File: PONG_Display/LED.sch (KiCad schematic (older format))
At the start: 4 parts, among them J1 LED_Display_Conn, U1 PC817

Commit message: 5v
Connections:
- net labels added: +5V
- net labels removed: +12V
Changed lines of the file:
@@
 EESchema Schematic File Version 4
-LIBS:PONG_Display-cache
 EELAYER 30 0
 EELAYER END
@@
 Schemat wyświetlacza LED
 $Comp
-L power:+12V #PWR0101
-U 1 1 5E85B748
-P 8500 2550
-F 0 "#PWR0101" H 8500 2400 50  0001 C CNN
-F 1 "+12V" H 8515 2723 50  0000 C CNN
-F 2 "" H 8500 2550 50  0001 C CNN
-F 3 "" H 8500 2550 50  0001 C CNN
-	1    8500 2550
-	1    0    0    -1
-$EndComp
-$Comp
-L power:GND #PWR0102
+L power:GND #PWR05
 U 1 1 5E85BD1D
 P 8500 3050
-F 0 "#PWR0102" H 8500 2800 50  0001 C CNN
+F 0 "#PWR05" H 8500 2800 50  0001 C CNN
 F 1 "GND" H 8505 2877 50  0000 C CNN
 F 2 "" H 8500 3050 50  0001 C CNN
@@
 $EndComp
 $Comp
-L power:GND #PWR0103
+L power:GND #PWR01
 U 1 1 5E9048A0
 P 2450 3200
-F 0 "#PWR0103" H 2450 2950 50  0001 C CNN
+F 0 "#PWR01" H 2450 2950 50  0001 C CNN
 F 1 "GND" H 2455 3027 50  0000 C CNN
 F 2 "" H 2450 3200 50  0001 C CNN
@@
 $EndComp
 $Comp
-L power:GND #PWR0105
+L power:GND #PWR02
 U 1 1 5E906F7A
 P 3400 3200
-F 0 "#PWR0105" H 3400 2950 50  0001 C CNN
+F 0 "#PWR02" H 3400 2950 50  0001 C CNN
 F 1 "GND" H 3405 3027 50  0000 C CNN
 F 2 "" H 3400 3200 50  0001 C CNN
@@
 	1900 2550 2050 2550
 $Comp
-L power:+12V #PWR0104
-U 1 1 5E9C9DE1
+L power:+5V #PWR?
+U 1 1 5EA0B092
+P 8500 2550
+AR Path="/5E80B14C/5EA0B092" Ref="#PWR?"  Part="1"
+AR Path="/5E80C133/5EA0B092" Ref="#PWR04"  Part="1"
+F 0 "#PWR04" H 8500 2400 50  0001 C CNN
+F 1 "+5V" H 8515 2723 50  0000 C CNN
+F 2 "" H 8500 2550 50  0001 C CNN
+F 3 "" H 8500 2550 50  0001 C CNN
+	1    8500 2550
+	1    0    0    -1
+$EndComp
+$Comp
+L power:+5V #PWR?
+U 1 1 5EA0B611
 P 3500 2300
-F 0 "#PWR0104" H 3500 2150 50  0001 C CNN
-F 1 "+12V" H 3515 2473 50  0000 C CNN
+AR Path="/5E80B14C/5EA0B611" Ref="#PWR?"  Part="1"
+AR Path="/5E80C133/5EA0B611" Ref="#PWR03"  Part="1"
+F 0 "#PWR03" H 3500 2150 50  0001 C CNN
+F 1 "+5V" H 3515 2473 50  0000 C CNN
 F 2 "" H 3500 2300 50  0001 C CNN
 F 3 "" H 3500 2300 50  0001 C CNN

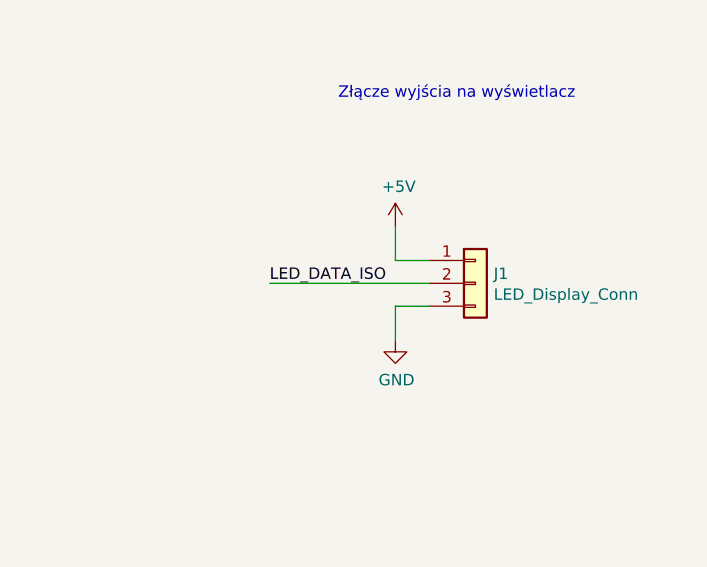
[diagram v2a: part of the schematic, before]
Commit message: dodalem rezystory i wywalilem ze zlacza zasilanie tasmy
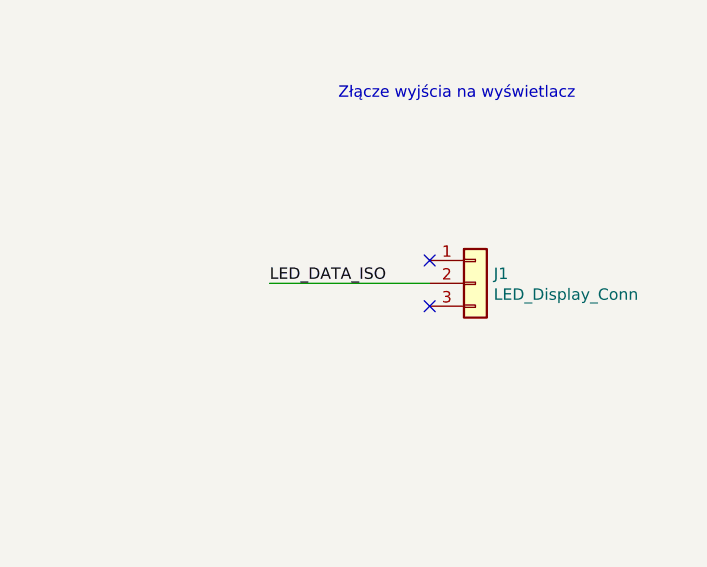
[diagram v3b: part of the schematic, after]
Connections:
- net +5V: no longer J1.1 (Pin_1)
- net GND: no longer J1.3 (Pin_3)
- no-connect marks 0 -> 2
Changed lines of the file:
@@
 Text Notes 7750 7500 0    50   ~ 0
 Schemat wyświetlacza LED
-$Comp
-L power:GND #PWR05
-U 1 1 5E85BD1D
-P 8500 3050
-F 0 "#PWR05" H 8500 2800 50  0001 C CNN
-F 1 "GND" H 8505 2877 50  0000 C CNN
-F 2 "" H 8500 3050 50  0001 C CNN
-F 3 "" H 8500 3050 50  0001 C CNN
-	1    8500 3050
-	1    0    0    -1
-$EndComp
-Wire Wire Line
-	8500 2550 8500 2700
-Wire Wire Line
-	8500 2700 8650 2700
-Wire Wire Line
-	8500 2900 8500 3050
-Wire Wire Line
-	8500 2900 8650 2900
 Text Notes 8250 2000 0    50   ~ 0
 Złącze wyjścia na wyświetlacz
@@
 $Comp
 L power:+5V #PWR?
-U 1 1 5EA0B092
-P 8500 2550
-AR Path="/5E80B14C/5EA0B092" Ref="#PWR?"  Part="1"
-AR Path="/5E80C133/5EA0B092" Ref="#PWR04"  Part="1"
-F 0 "#PWR04" H 8500 2400 50  0001 C CNN
-F 1 "+5V" H 8515 2723 50  0000 C CNN
-F 2 "" H 8500 2550 50  0001 C CNN
-F 3 "" H 8500 2550 50  0001 C CNN
-	1    8500 2550
-	1    0    0    -1
-$EndComp
-$Comp
-L power:+5V #PWR?
 U 1 1 5EA0B611
 P 3500 2300
@@
 	1    0    0    -1
 $EndComp
+NoConn ~ 8650 2700
+NoConn ~ 8650 2900
 $EndSCHEMATC

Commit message: layout v1
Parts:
- C1: footprint Capacitor_SMD:C_1206_3216Metric_Pad1.42x1.75mm_HandSolder -> Capacitor_SMD:C_0603_1608Metric_Pad1.05x0.95mm_HandSolder
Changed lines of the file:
@@
 EESchema Schematic File Version 4
-LIBS:PONG_Display-cache
 EELAYER 30 0
 EELAYER END
@@
 F 0 "C1" H 3515 2996 50  0000 L CNN
 F 1 "100n" H 3515 2905 50  0000 L CNN
-F 2 "Capacitor_SMD:C_1206_3216Metric_Pad1.42x1.75mm_HandSolder" H 3438 2800 50  0001 C CNN
+F 2 "Capacitor_SMD:C_0603_1608Metric_Pad1.05x0.95mm_HandSolder" H 3438 2800 50  0001 C CNN
 F 3 "~" H 3400 2950 50  0001 C CNN
 	1    3400 2950

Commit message: l
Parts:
- R1: footprint Resistor_SMD:R_1206_3216Metric_Pad1.42x1.75mm_HandSolder -> Resistor_SMD:R_0603_1608Metric_Pad1.05x0.95mm_HandSolder
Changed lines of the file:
@@
 F 0 "R1" V 1993 2550 50  0000 C CNN
 F 1 "180R" V 2084 2550 50  0000 C CNN
-F 2 "Resistor_SMD:R_1206_3216Metric_Pad1.42x1.75mm_HandSolder" V 2130 2550 50  0001 C CNN
+F 2 "Resistor_SMD:R_0603_1608Metric_Pad1.05x0.95mm_HandSolder" V 2130 2550 50  0001 C CNN
 F 3 "~" H 2200 2550 50  0001 C CNN
 	1    2200 2550

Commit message: layout4
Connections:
- net GND: now also J1.1 (Pin_1)
- net +5VA: now reaches J1.3 (Pin_3)
- no-connect marks 2 -> 0
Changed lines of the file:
@@
 F 3 "~" H 8850 2800 50  0001 C CNN
 	1    8850 2800
-	1    0    0    -1
+	1    0    0    1
 $EndComp
 Text Notes 7750 7500 0    50   ~ 0
@@
 	1    0    0    -1
 $EndComp
-NoConn ~ 8650 2700
-NoConn ~ 8650 2900
+$Comp
+L power:GND #PWR0109
+U 1 1 5EB33F3E
+P 8600 3100
+F 0 "#PWR0109" H 8600 2850 50  0001 C CNN
+F 1 "GND" H 8605 2927 50  0000 C CNN
+F 2 "" H 8600 3100 50  0001 C CNN
+F 3 "" H 8600 3100 50  0001 C CNN
+	1    8600 3100
+	1    0    0    -1
+$EndComp
+Wire Wire Line
+	8600 2500 8600 2700
+Wire Wire Line
+	8600 2700 8650 2700
+Wire Wire Line
+	8600 3100 8600 2900
+Wire Wire Line
+	8600 2900 8650 2900
+$Comp
+L power:+5VA #PWR0110
+U 1 1 5EA4877F
+P 8600 2500
+F 0 "#PWR0110" H 8600 2350 50  0001 C CNN
+F 1 "+5VA" H 8615 2673 50  0000 C CNN
+F 2 "" H 8600 2500 50  0001 C CNN
+F 3 "" H 8600 2500 50  0001 C CNN
+	1    8600 2500
+	1    0    0    -1
+$EndComp
 $EndSCHEMATC

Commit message: laayout6
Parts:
- J1: footprint TerminalBlock:TerminalBlock_bornier-3_P5.08mm -> TerminalBlock_RND:TerminalBlock_RND_205-00002_1x03_P5.00mm_Horizontal
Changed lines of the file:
@@
 F 0 "J1" H 8930 2842 50  0000 L CNN
 F 1 "LED_Display_Conn" H 8930 2751 50  0000 L CNN
-F 2 "TerminalBlock:TerminalBlock_bornier-3_P5.08mm" H 8850 2800 50  0001 C CNN
+F 2 "TerminalBlock_RND:TerminalBlock_RND_205-00002_1x03_P5.00mm_Horizontal" H 8850 2800 50  0001 C CNN
 F 3 "~" H 8850 2800 50  0001 C CNN
 	1    8850 2800
